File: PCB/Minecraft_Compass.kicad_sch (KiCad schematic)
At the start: 63 parts, among them SW1 1825910-6, U1 TLC5947DAP, U2 TLC5947DAP, U3 TLC5947DAP, U4 LC86G, U5 LIS3MDL

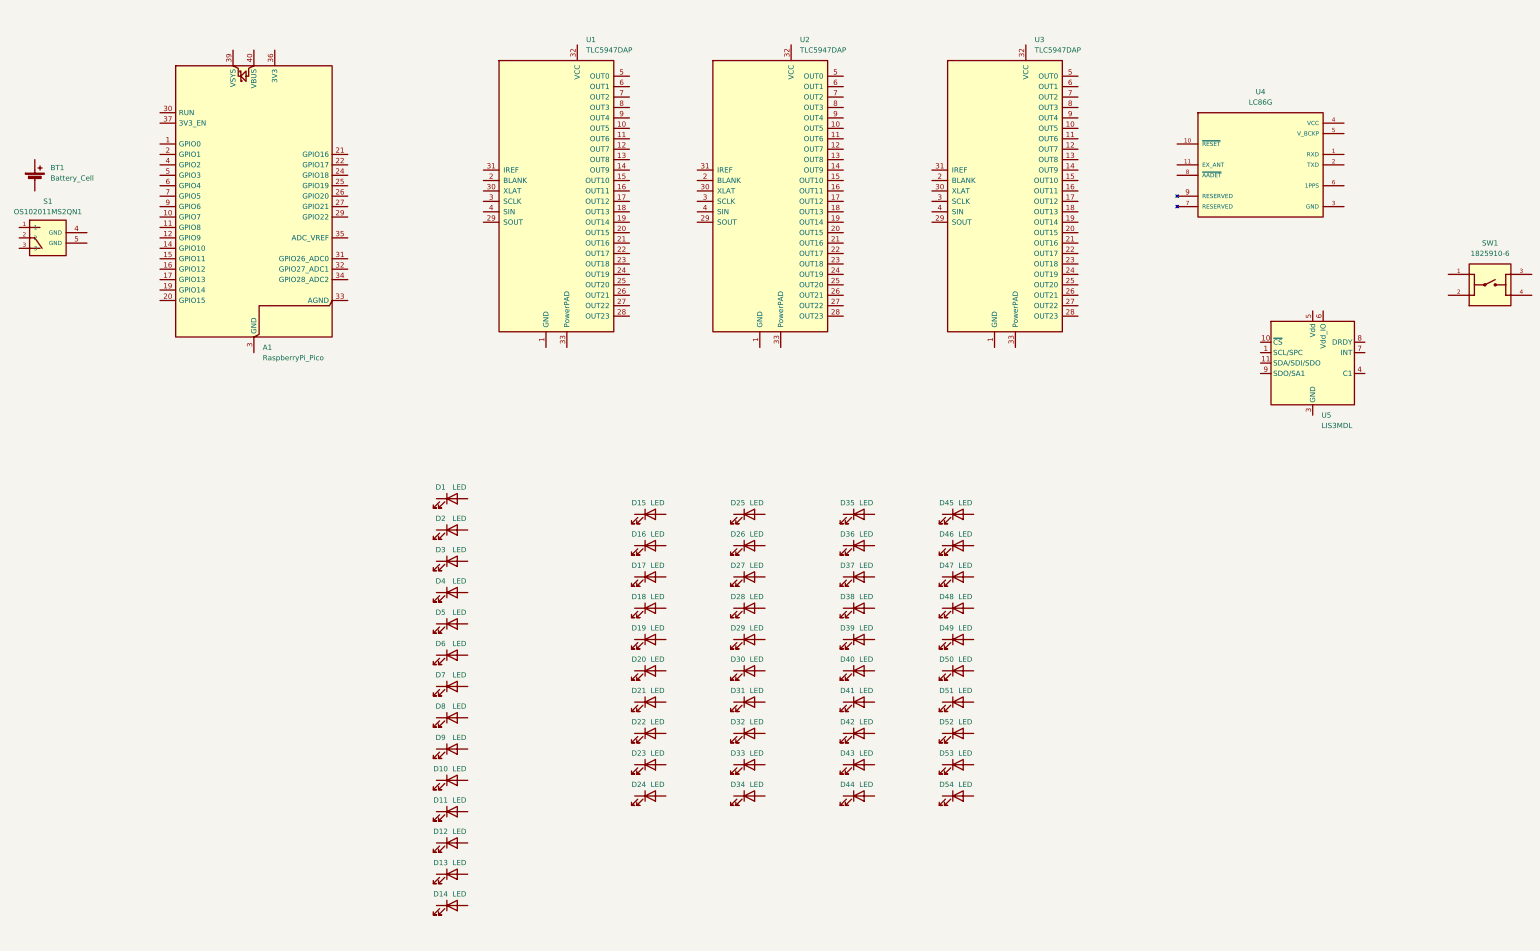
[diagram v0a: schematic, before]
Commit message: Update LED Setup
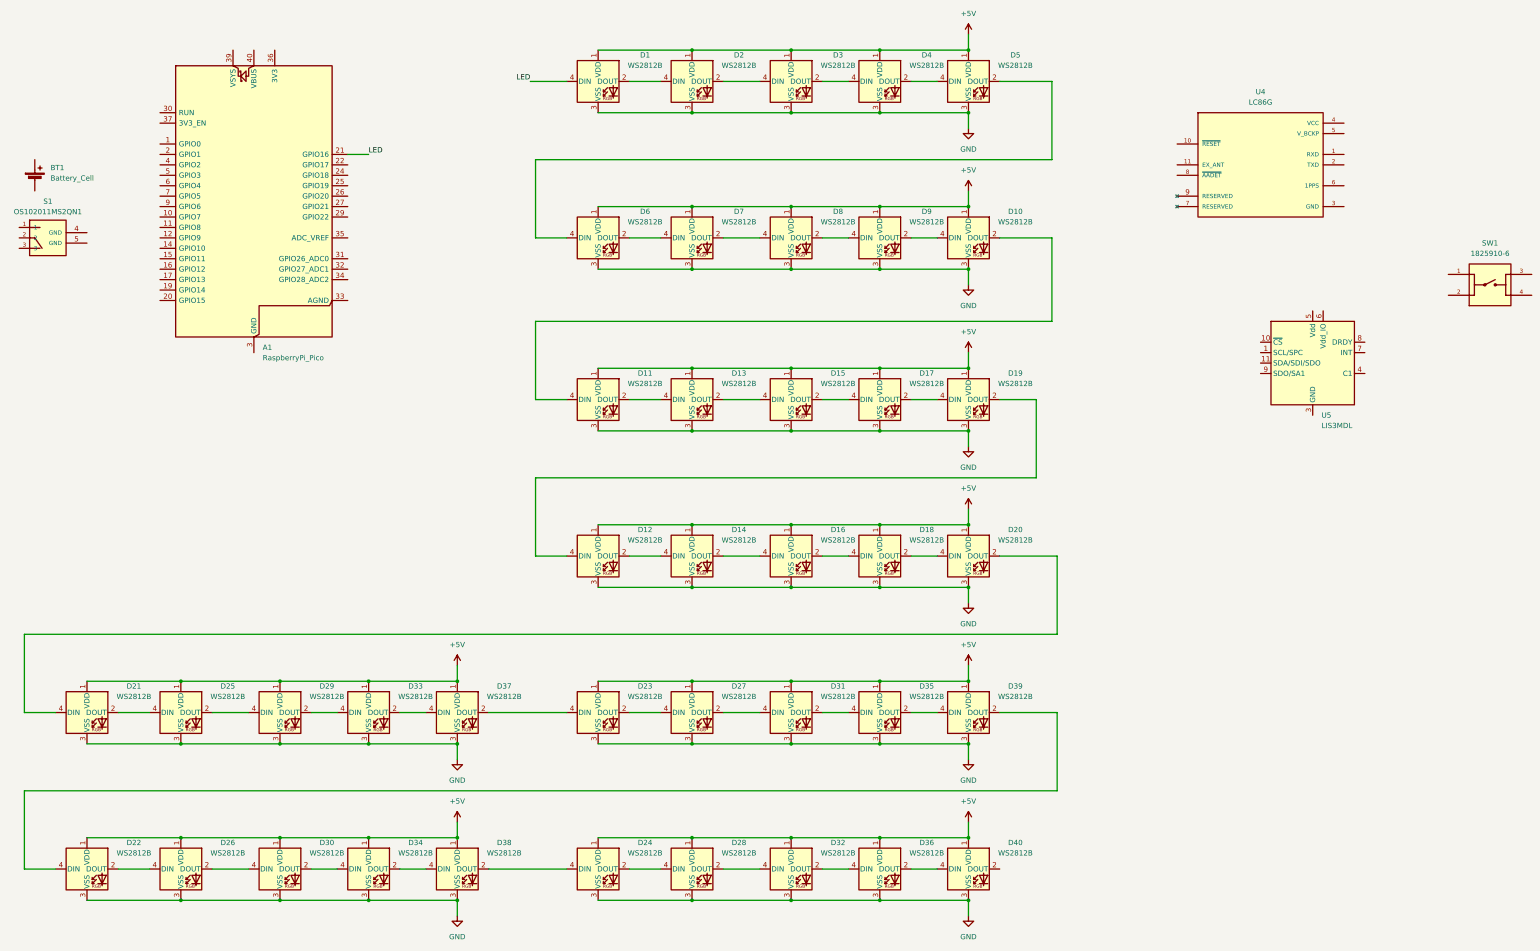
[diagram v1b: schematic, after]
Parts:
- removed D1, D10, D11, D12, D13, D14, D15, D16, D17, D18, D19, D2, D20, D21, D22, D23, D24, D25, D26, D27, D28, D29, D3, D30, D31, D32, D33, D34, D35, D36, D37, D38, D39, D4, D40, D41, D42, D43, D44, D45, D46, D47, D48, D49, D5, D50, D51, D52, D53, D54, D6, D7, D8, D9: LED, symbol Device:LED
- removed U1, U2, U3: TLC5947DAP, Package_SO:HTSSOP-32-1EP_6.1x11mm_P0.65mm_EP5.2x11mm_Mask4.11x4.36mm_ThermalVias, symbol Driver_LED:TLC5947DAP
- added D1, D10, D11, D12, D13, D14, D15, D16, D17, D18, D19, D2, D20, D21, D22, D23, D24, D25, D26, D27, D28, D29, D3, D30, D31, D32, D33, D34, D35, D36, D37, D38, D39, D4, D40, D5, D6, D7, D8, D9: WS2812B, LED_SMD:LED_WS2812B_PLCC4_5.0x5.0mm_P3.2mm, symbol LED:WS2812B
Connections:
- net LED: now reaches A1.21 (GPIO16)
- net LED: now also D1.4 (DIN)
- new net: D20.2 (DOUT), D21.4 (DIN)
- new net: D18.2 (DOUT), D20.4 (DIN)
- new net: D25.2 (DOUT), D29.4 (DIN)
- new net: D21.2 (DOUT), D25.4 (DIN)
- new net: D16.2 (DOUT), D18.4 (DIN)
- new net: D32.2 (DOUT), D36.4 (DIN)
- new net: D28.2 (DOUT), D32.4 (DIN)
- new net: D30.2 (DOUT), D34.4 (DIN)
- new net: D26.2 (DOUT), D30.4 (DIN)
- new net: D17.2 (DOUT), D19.4 (DIN)
- new net: D15.2 (DOUT), D17.4 (DIN)
- new net: D36.2 (DOUT), D40.4 (DIN)
- new net: D2.2 (DOUT), D3.4 (DIN)
- new net: D1.2 (DOUT), D2.4 (DIN)
- new net: D3.2 (DOUT), D4.4 (DIN)
- new net: D24.2 (DOUT), D28.4 (DIN)
- new net: D24.4 (DIN), D38.2 (DOUT)
- new net: D12.4 (DIN), D19.2 (DOUT)
- new net: D11.2 (DOUT), D13.4 (DIN)
- new net: D10.2 (DOUT), D11.4 (DIN)
- new net: D4.2 (DOUT), D5.4 (DIN)
- new net: D22.2 (DOUT), D26.4 (DIN)
- new net: D34.2 (DOUT), D38.4 (DIN)
- new net: D22.4 (DIN), D39.2 (DOUT)
- new net: D35.2 (DOUT), D39.4 (DIN)
- new net: D12.2 (DOUT), D14.4 (DIN)
- new net: D27.2 (DOUT), D31.4 (DIN)
- new net: D23.2 (DOUT), D27.4 (DIN)
- new net: D33.2 (DOUT), D37.4 (DIN)
- new net: D29.2 (DOUT), D33.4 (DIN)
- new net: D13.2 (DOUT), D15.4 (DIN)
- new net: D14.2 (DOUT), D16.4 (DIN)
- new net: D23.4 (DIN), D37.2 (DOUT)
- new net: D8.2 (DOUT), D9.4 (DIN)
- new net: D7.2 (DOUT), D8.4 (DIN)
- new net: D10.4 (DIN), D9.2 (DOUT)
- new net: D31.2 (DOUT), D35.4 (DIN)
- new net: D6.2 (DOUT), D7.4 (DIN)
- new net: D5.2 (DOUT), D6.4 (DIN)
- new net +5V: D1.1 (VDD), D10.1 (VDD), D11.1 (VDD), D12.1 (VDD), D13.1 (VDD), D14.1 (VDD), D15.1 (VDD), D16.1 (VDD), D17.1 (VDD), D18.1 (VDD), D19.1 (VDD), D2.1 (VDD), D20.1 (VDD), D21.1 (VDD), D22.1 (VDD), D23.1 (VDD), D24.1 (VDD), D25.1 (VDD), D26.1 (VDD), D27.1 (VDD), D28.1 (VDD), D29.1 (VDD), D3.1 (VDD), D30.1 (VDD), D31.1 (VDD), D32.1 (VDD), D33.1 (VDD), D34.1 (VDD), D35.1 (VDD), D36.1 (VDD), D37.1 (VDD), D38.1 (VDD), D39.1 (VDD), D4.1 (VDD), D40.1 (VDD), D5.1 (VDD), D6.1 (VDD), D7.1 (VDD), D8.1 (VDD), D9.1 (VDD)
- new net GND: D1.3 (VSS), D10.3 (VSS), D11.3 (VSS), D12.3 (VSS), D13.3 (VSS), D14.3 (VSS), D15.3 (VSS), D16.3 (VSS), D17.3 (VSS), D18.3 (VSS), D19.3 (VSS), D2.3 (VSS), D20.3 (VSS), D21.3 (VSS), D22.3 (VSS), D23.3 (VSS), D24.3 (VSS), D25.3 (VSS), D26.3 (VSS), D27.3 (VSS), D28.3 (VSS), D29.3 (VSS), D3.3 (VSS), D30.3 (VSS), D31.3 (VSS), D32.3 (VSS), D33.3 (VSS), D34.3 (VSS), D35.3 (VSS), D36.3 (VSS), D37.3 (VSS), D38.3 (VSS), D39.3 (VSS), D4.3 (VSS), D40.3 (VSS), D5.3 (VSS), D6.3 (VSS), D7.3 (VSS), D8.3 (VSS), D9.3 (VSS)
